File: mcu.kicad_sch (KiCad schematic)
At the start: 1 part

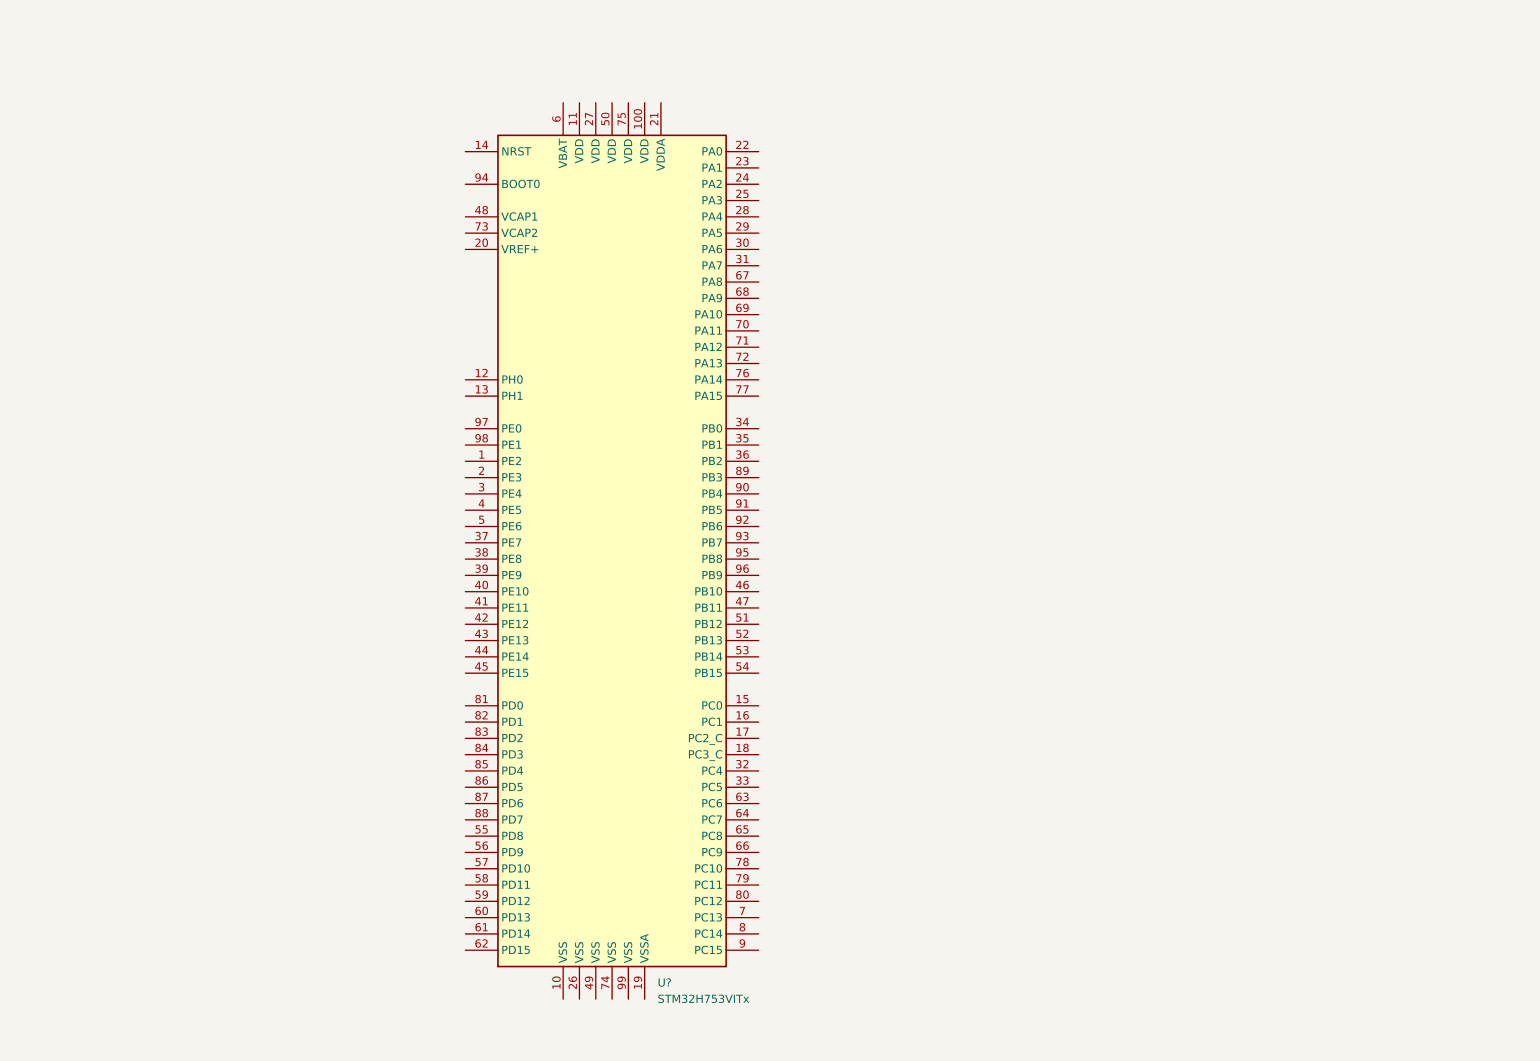
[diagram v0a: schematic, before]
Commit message: Create scheme for MCU with peripheries
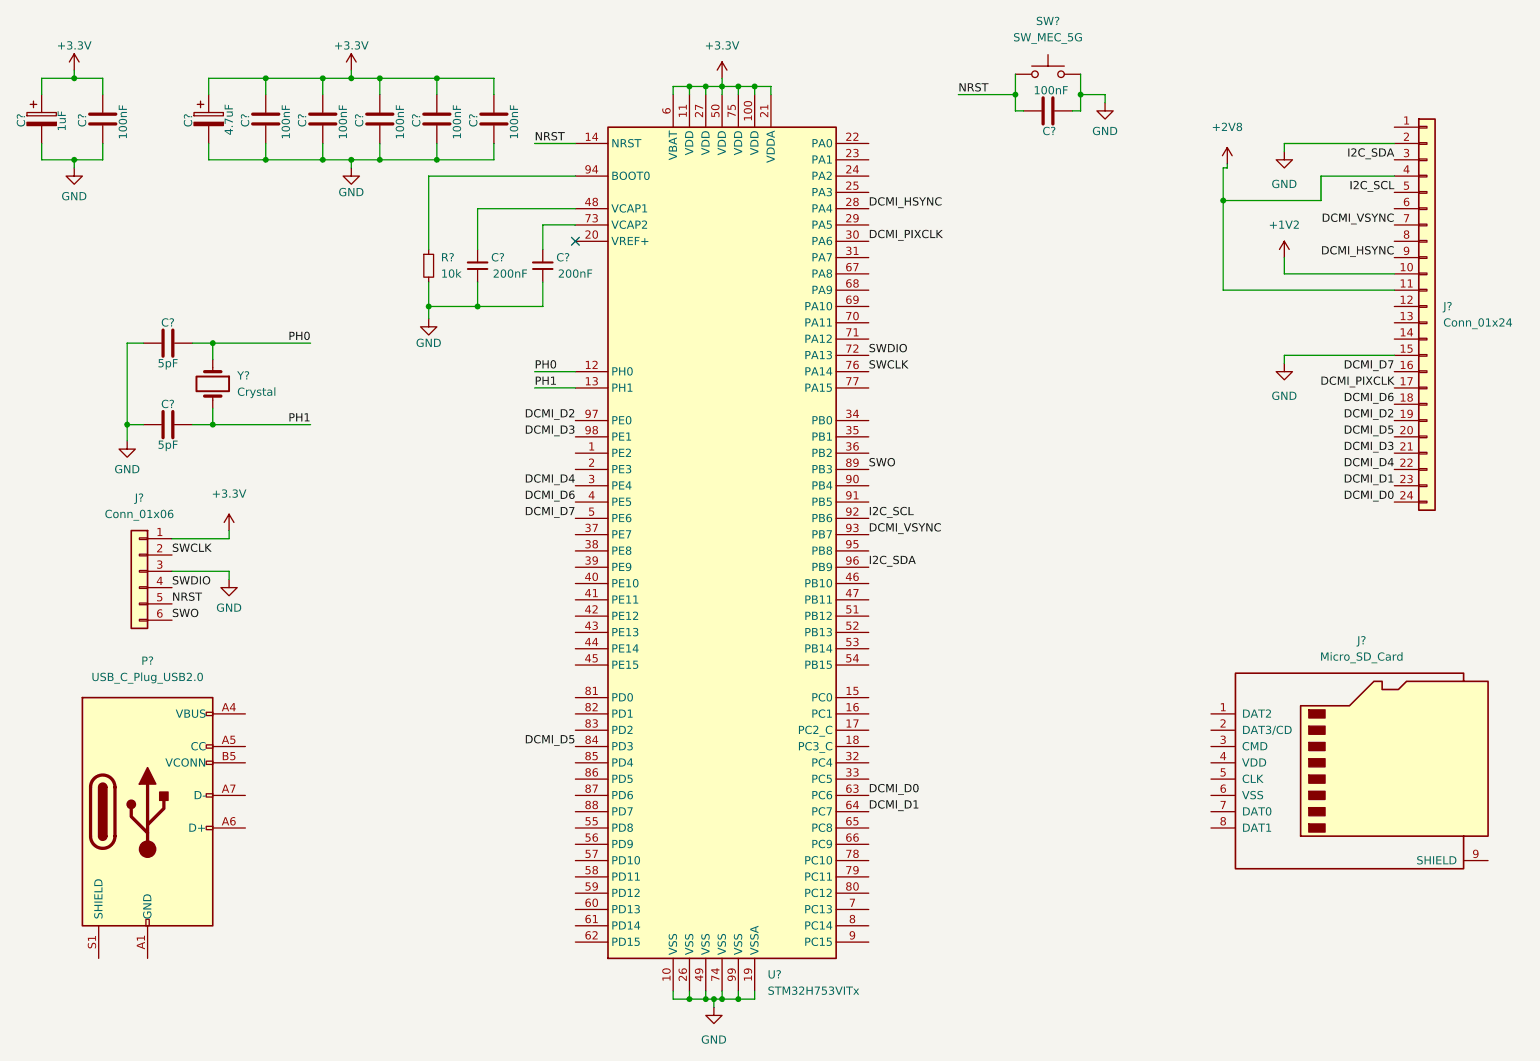
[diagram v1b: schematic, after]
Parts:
- added C? (x7): 100nF, symbol Device:C
- added C? (x2): 200nF, symbol Device:C_Small
- added C?: 1uF, symbol Device:C_Polarized
- added C? (x2): 5pF, symbol Device:C
- added C?: 4.7uF, symbol Device:C_Polarized
- added J?: Micro_SD_Card, symbol Connector:Micro_SD_Card
- added J?: Conn_01x24, symbol Connector_Generic:Conn_01x24
- added J?: Conn_01x06, symbol Connector_Generic:Conn_01x06
- added P?: USB_C_Plug_USB2.0, symbol Connector:USB_C_Plug_USB2.0
- added R?: 10k, symbol Device:R_Small
- added SW?: SW_MEC_5G, symbol Switch:SW_MEC_5G
- added Y?: Crystal, symbol Device:Crystal
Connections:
- net GND: now reaches U?.10 (VSS)
- net GND: now also U?.19 (VSSA), U?.26 (VSS), U?.49 (VSS), U?.74 (VSS), U?.99 (VSS), C?.1, C?.1, C?.1, C?.1, C?.2, C?.2, C?.2, C?.2, C?.2, C?.2, C?.2, C?.2, C?.2, J?.15 (Pin_15), J?.2 (Pin_2), J?.3 (Pin_3), R?.2, SW?.3 (B), SW?.4 (B)
- net +3V3: now reaches U?.100 (VDD)
- net +3V3: now also U?.11 (VDD), U?.21 (VDDA), U?.27 (VDD), U?.50 (VDD), U?.6 (VBAT), U?.75 (VDD), C?.1, C?.1, C?.1, C?.1, C?.1, C?.1, C?.1, C?.1, J?.1 (Pin_1)
- net PH0: now reaches U?.12 (PH0)
- net PH0: now also C?.2, Y?.1
- net PH1: now reaches U?.13 (PH1)
- net PH1: now also C?.2, Y?.2
- net NRST: now reaches U?.14 (NRST)
- net NRST: now also C?.1, J?.5 (Pin_5), SW?.1 (A), SW?.2 (A)
- net DCMI_HSYNC: now reaches U?.28 (PA4)
- net DCMI_HSYNC: now also J?.9 (Pin_9)
- net DCMI_D4: now reaches U?.3 (PE4)
- net DCMI_D4: now also J?.22 (Pin_22)
- net DCMI_PIXCLK: now reaches U?.30 (PA6)
- net DCMI_PIXCLK: now also J?.17 (Pin_17)
- net DCMI_D6: now reaches U?.4 (PE5)
- net DCMI_D6: now also J?.18 (Pin_18)
- net at U?.48 (VCAP1): now also C?.2
- net DCMI_D7: now reaches U?.5 (PE6)
- net DCMI_D7: now also J?.16 (Pin_16)
- net DCMI_D0: now reaches U?.63 (PC6)
- net DCMI_D0: now also J?.24 (Pin_24)
- net DCMI_D1: now reaches U?.64 (PC7)
- net DCMI_D1: now also J?.23 (Pin_23)
- net SWDIO: now reaches U?.72 (PA13)
- net SWDIO: now also J?.4 (Pin_4)
- net at U?.73 (VCAP2): now also C?.2
- net SWCLK: now reaches U?.76 (PA14)
- net SWCLK: now also J?.2 (Pin_2)
- net DCMI_D5: now reaches U?.84 (PD3)
- net DCMI_D5: now also J?.20 (Pin_20)
- net SWO: now reaches U?.89 (PB3)
- net SWO: now also J?.6 (Pin_6)
- net I2C_SCL: now reaches U?.92 (PB6)
- net I2C_SCL: now also J?.5 (Pin_5)
- net DCMI_VSYNC: now reaches U?.93 (PB7)
- net DCMI_VSYNC: now also J?.7 (Pin_7)
- net at U?.94 (BOOT0): now also R?.1
- net I2C_SDA: now reaches U?.96 (PB9)
- net I2C_SDA: now also J?.3 (Pin_3)
- net DCMI_D2: now reaches U?.97 (PE0)
- net DCMI_D2: now also J?.19 (Pin_19)
- net DCMI_D3: now reaches U?.98 (PE1)
- net DCMI_D3: now also J?.21 (Pin_21)
- new net: P?.A1 (GND), P?.A12 (GND), P?.B1 (GND), P?.B12 (GND)
- new net: P?.A4 (VBUS), P?.A9 (VBUS), P?.B4 (VBUS), P?.B9 (VBUS)
- new net +1V2: J?.10 (Pin_10)
- new net +2V8: J?.11 (Pin_11), J?.4 (Pin_4)
- no-connect marks 0 -> 1
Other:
- moved on the sheet: U?
